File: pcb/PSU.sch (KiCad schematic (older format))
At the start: 18 parts, among them Q3 DMG2305UX, Q4 BCM857BS, U18 XCL206B123, U9 AP7361C-33-FGE

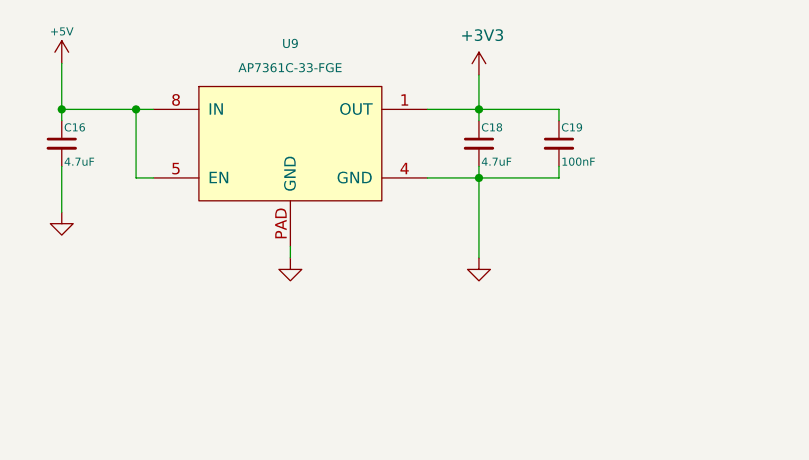
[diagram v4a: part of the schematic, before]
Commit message: 3v3 torex reg
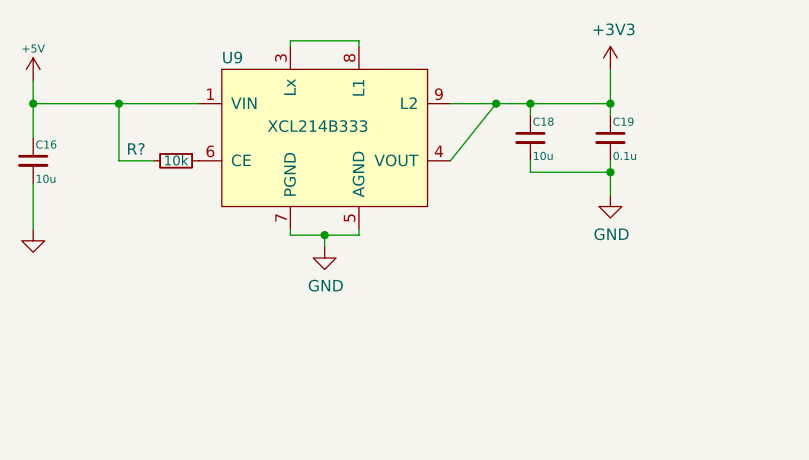
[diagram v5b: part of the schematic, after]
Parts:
- removed U9: AP7361C-33-FGE, SMD:8DFN, symbol ap7361c:AP7361C-33-ap7361c-33
- added R?: 10k, Resistor_SMD:R_0402_1005Metric, symbol Device:R_Small
- added U9: XCL214B333, symbol torex:XCL214
- C16, C18: value 4.7uF -> 10u
- C19: value 100nF -> 0.1u
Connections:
- net +3V3: now also U9.4 (VOUT), U9.9 (L2)
- net +5V: now also R?.2, U9.1 (VIN)
- net GND: now also U9.5 (AGND), U9.7 (PGND)
- new net: U9.3 (Lx), U9.8 (L1)
- new net: R?.1, U9.6 (CE)
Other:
- moved on the sheet: C16, C18, C19
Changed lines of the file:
@@
 L power:+5V #PWR0111
 U 1 1 590BB025
-P 1750 1800
-F 0 "#PWR0111" H 1750 1650 35  0001 C CNN
-F 1 "+5V" H 1750 1940 35  0000 C CNN
-F 2 "" H 1750 1800 60  0000 C CNN
-F 3 "" H 1750 1800 60  0000 C CNN
-	1    1750 1800
-	1    0    0    -1
-$EndComp
-$Comp
-L Device:C_Small C18
-U 1 1 590BB02B
-P 3575 2150
-F 0 "C18" H 3585 2220 35  0000 L CNN
-F 1 "4.7uF" H 3585 2070 35  0000 L CNN
-F 2 "Capacitors_SMD:C_0603" H 3575 2150 60  0001 C CNN
-F 3 "" H 3575 2150 60  0000 C CNN
-	1    3575 2150
-	1    0    0    -1
-$EndComp
-$Comp
-L power:GND #PWR0112
-U 1 1 590BB032
-P 3575 2650
-F 0 "#PWR0112" H 3575 2650 30  0001 C CNN
-F 1 "GND" H 3575 2580 30  0001 C CNN
-F 2 "" H 3575 2650 60  0000 C CNN
-F 3 "" H 3575 2650 60  0000 C CNN
-	1    3575 2650
+P 1625 1875
+F 0 "#PWR0111" H 1625 1725 35  0001 C CNN
+F 1 "+5V" H 1625 2015 35  0000 C CNN
+F 2 "" H 1625 1875 60  0000 C CNN
+F 3 "" H 1625 1875 60  0000 C CNN
+	1    1625 1875
 	1    0    0    -1
 $EndComp
@@
 L power:GND #PWR0116
 U 1 1 590BB038
-P 1750 2450
-F 0 "#PWR0116" H 1750 2450 30  0001 C CNN
-F 1 "GND" H 1750 2380 30  0001 C CNN
-F 2 "" H 1750 2450 60  0000 C CNN
-F 3 "" H 1750 2450 60  0000 C CNN
-	1    1750 2450
+P 1625 2525
+F 0 "#PWR0116" H 1625 2525 30  0001 C CNN
+F 1 "GND" H 1625 2455 30  0001 C CNN
+F 2 "" H 1625 2525 60  0000 C CNN
+F 3 "" H 1625 2525 60  0000 C CNN
+	1    1625 2525
 	1    0    0    -1
 $EndComp
@@
 L Device:C_Small C16
 U 1 1 590BB03E
-P 1750 2150
-F 0 "C16" H 1760 2220 35  0000 L CNN
-F 1 "4.7uF" H 1760 2070 35  0000 L CNN
-F 2 "Capacitors_SMD:C_0603" H 1750 2150 60  0001 C CNN
-F 3 "" H 1750 2150 60  0000 C CNN
-	1    1750 2150
-	1    0    0    -1
-$EndComp
-$Comp
-L power:GND #PWR0117
-U 1 1 590BB04C
-P 2750 2650
-F 0 "#PWR0117" H 2750 2650 30  0001 C CNN
-F 1 "GND" H 2750 2580 30  0001 C CNN
-F 2 "" H 2750 2650 60  0000 C CNN
-F 3 "" H 2750 2650 60  0000 C CNN
-	1    2750 2650
-	1    0    0    -1
-$EndComp
-$Comp
-L Device:C_Small C19
-U 1 1 590BB065
-P 3925 2150
-F 0 "C19" H 3935 2220 35  0000 L CNN
-F 1 "100nF" H 3935 2070 35  0000 L CNN
-F 2 "Capacitors_SMD:C_0402" H 3925 2150 60  0001 C CNN
-F 3 "" H 3925 2150 60  0000 C CNN
-	1    3925 2150
-	1    0    0    -1
-$EndComp
-$Comp
-L ap7361c:AP7361C-33-ap7361c-33 U9
-U 1 1 590BB045
-P 2750 2200
-F 0 "U9" H 2750 2687 39  0000 C CNN
-F 1 "AP7361C-33-FGE" H 2750 2581 39  0000 C CNN
-F 2 "SMD:8DFN" H 2700 2200 60  0001 C CNN
-F 3 "" H 2700 2200 60  0001 C CNN
-	1    2750 2200
+P 1625 2225
+F 0 "C16" H 1635 2295 35  0000 L CNN
+F 1 "10u" H 1635 2145 35  0000 L CNN
+F 2 "Capacitors_SMD:C_0603" H 1625 2225 60  0001 C CNN
+F 3 "" H 1625 2225 60  0000 C CNN
+	1    1625 2225
 	1    0    0    -1
 $EndComp
@@
 	1    0    0    -1
 $EndComp
-Connection ~ 1750 2000
-Wire Wire Line
-	1750 2000 2075 2000
-Wire Wire Line
-	1750 1800 1750 2000
-Connection ~ 3575 2000
-Wire Wire Line
-	3575 1850 3575 2000
-Connection ~ 3575 2300
-Wire Wire Line
-	3350 2300 3575 2300
-Wire Wire Line
-	3575 2250 3575 2300
-Wire Wire Line
-	2750 2600 2750 2650
-Wire Wire Line
-	1750 2250 1750 2450
-Wire Wire Line
-	2150 2300 2075 2300
-Wire Wire Line
-	2075 2300 2075 2000
-Connection ~ 2075 2000
-Wire Wire Line
-	3350 2000 3575 2000
-Wire Wire Line
-	3925 2300 3925 2250
-Wire Wire Line
-	3925 2050 3925 2000
+Wire Wire Line
+	1625 2325 1625 2525
 Wire Wire Line
 	1900 4875 2050 4875
@@
 	5050 4950 5050 4900
 Wire Wire Line
-	1750 2000 1750 2050
-Wire Wire Line
-	3575 2000 3575 2050
-Wire Wire Line
-	3575 2000 3925 2000
-Wire Wire Line
-	3575 2300 3925 2300
-Wire Wire Line
-	3575 2300 3575 2650
-Wire Wire Line
-	2075 2000 2150 2000
-Wire Wire Line
 	2675 4875 2750 4875
 Wire Wire Line
@@
 L power:+3V3 #PWR0224
 U 1 1 5EA96191
-P 3575 1850
-F 0 "#PWR0224" H 3575 1700 50  0001 C CNN
-F 1 "+3V3" H 3590 2023 50  0000 C CNN
-F 2 "" H 3575 1850 50  0001 C CNN
-F 3 "" H 3575 1850 50  0001 C CNN
-	1    3575 1850
+P 4150 1825
+F 0 "#PWR0224" H 4150 1675 50  0001 C CNN
+F 1 "+3V3" H 4165 1998 50  0000 C CNN
+F 2 "" H 4150 1825 50  0001 C CNN
+F 3 "" H 4150 1825 50  0001 C CNN
+	1    4150 1825
 	1    0    0    -1
 $EndComp
@@
 Wire Wire Line
 	6550 1900 6550 1925
+$Comp
+L torex:XCL214 U9
+U 1 1 5EE15428
+P 2900 2125
+F 0 "U9" H 2450 2475 50  0000 L CNN
+F 1 "XCL214B333" H 2650 2175 50  0000 L CNN
+F 2 "" H 2900 2125 50  0001 C CNN
+F 3 "" H 2900 2125 50  0001 C CNN
+F 4 " 893-1218-6-ND " H 2900 2125 50  0001 C CNN "DigiKey"
+	1    2900 2125
+	1    0    0    -1
+$EndComp
+Wire Wire Line
+	3450 1975 3650 1975
+Wire Wire Line
+	3450 2225 3650 1975
+Wire Wire Line
+	2750 1725 2750 1700
+Wire Wire Line
+	2750 1700 3050 1700
+Wire Wire Line
+	3050 1700 3050 1725
+Wire Wire Line
+	2750 2525 2750 2550
+Wire Wire Line
+	2750 2550 2900 2550
+Wire Wire Line
+	3050 2550 3050 2525
+Wire Wire Line
+	2900 2550 2900 2600
+Connection ~ 2900 2550
+Wire Wire Line
+	2900 2550 3050 2550
+$Comp
+L power:GND #PWR?
+U 1 1 5EE35BB4
+P 2900 2600
+F 0 "#PWR?" H 2900 2350 50  0001 C CNN
+F 1 "GND" H 2905 2427 50  0000 C CNN
+F 2 "" H 2900 2600 50  0001 C CNN
+F 3 "" H 2900 2600 50  0001 C CNN
+	1    2900 2600
+	1    0    0    -1
+$EndComp
+$Comp
+L Device:C_Small C18
+U 1 1 590BB02B
+P 3800 2125
+F 0 "C18" H 3810 2195 35  0000 L CNN
+F 1 "10u" H 3810 2045 35  0000 L CNN
+F 2 "Capacitors_SMD:C_0603" H 3800 2125 60  0001 C CNN
+F 3 "" H 3800 2125 60  0000 C CNN
+	1    3800 2125
+	1    0    0    -1
+$EndComp
+Wire Wire Line
+	3800 1975 3800 2025
+Wire Wire Line
+	3800 2275 4150 2275
+Wire Wire Line
+	3800 1975 4150 1975
+Wire Wire Line
+	4150 2025 4150 1975
+Wire Wire Line
+	4150 2275 4150 2225
+Wire Wire Line
+	3800 2225 3800 2275
+Connection ~ 4150 1975
+Wire Wire Line
+	4150 1825 4150 1975
+$Comp
+L Device:C_Small C19
+U 1 1 590BB065
+P 4150 2125
+F 0 "C19" H 4160 2195 35  0000 L CNN
+F 1 "0.1u" H 4160 2045 35  0000 L CNN
+F 2 "Capacitors_SMD:C_0402" H 4150 2125 60  0001 C CNN
+F 3 "" H 4150 2125 60  0000 C CNN
+	1    4150 2125
+	1    0    0    -1
+$EndComp
+Wire Wire Line
+	3650 1975 3800 1975
+Connection ~ 3650 1975
+Connection ~ 3800 1975
+Wire Wire Line
+	4150 2275 4150 2375
+Connection ~ 4150 2275
+$Comp
+L power:GND #PWR?
+U 1 1 5EE597F6
+P 4150 2375
+F 0 "#PWR?" H 4150 2125 50  0001 C CNN
+F 1 "GND" H 4155 2202 50  0000 C CNN
+F 2 "" H 4150 2375 50  0001 C CNN
+F 3 "" H 4150 2375 50  0001 C CNN
+	1    4150 2375
+	1    0    0    -1
+$EndComp
+$Comp
+L Device:R_Small R?
+U 1 1 5EE5CC96
+P 2250 2225
+F 0 "R?" V 2200 2050 50  0000 C CNN
+F 1 "10k" V 2250 2225 43  0000 C CNN
+F 2 "Resistor_SMD:R_0402_1005Metric" H 2250 2225 50  0001 C CNN
+F 3 "~" H 2250 2225 50  0001 C CNN
+	1    2250 2225
+	0    1    1    0
+$EndComp
+Wire Wire Line
+	2000 2225 2150 2225
+Wire Wire Line
+	2350 1975 2000 1975
+Wire Wire Line
+	2000 1975 2000 2225
+Wire Wire Line
+	1625 1875 1625 1975
+Wire Wire Line
+	2000 1975 1625 1975
+Connection ~ 2000 1975
+Connection ~ 1625 1975
+Wire Wire Line
+	1625 1975 1625 2125
 $EndSCHEMATC

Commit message: torex dc-dc module
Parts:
- U9: footprint (none) -> SMD:TOREX_XCL214B123DR
- gave numbers to parts that had none: 1
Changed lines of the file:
@@
 EESchema Schematic File Version 4
+LIBS:keep_breathing_ctrl-cache
 EELAYER 30 0
 EELAYER END
@@
 F 0 "U9" H 2450 2475 50  0000 L CNN
 F 1 "XCL214B333" H 2650 2175 50  0000 L CNN
-F 2 "" H 2900 2125 50  0001 C CNN
+F 2 "SMD:TOREX_XCL214B123DR" H 2900 2125 50  0001 C CNN
 F 3 "" H 2900 2125 50  0001 C CNN
 F 4 " 893-1218-6-ND " H 2900 2125 50  0001 C CNN "DigiKey"
@@
 	2900 2550 3050 2550
 $Comp
-L power:GND #PWR?
+L power:GND #PWR0112
 U 1 1 5EE35BB4
 P 2900 2600
-F 0 "#PWR?" H 2900 2350 50  0001 C CNN
+F 0 "#PWR0112" H 2900 2350 50  0001 C CNN
 F 1 "GND" H 2905 2427 50  0000 C CNN
 F 2 "" H 2900 2600 50  0001 C CNN
@@
 Connection ~ 4150 2275
 $Comp
-L power:GND #PWR?
+L power:GND #PWR0117
 U 1 1 5EE597F6
 P 4150 2375
-F 0 "#PWR?" H 4150 2125 50  0001 C CNN
+F 0 "#PWR0117" H 4150 2125 50  0001 C CNN
 F 1 "GND" H 4155 2202 50  0000 C CNN
 F 2 "" H 4150 2375 50  0001 C CNN
@@
 $EndComp
 $Comp
-L Device:R_Small R?
+L Device:R_Small R43
 U 1 1 5EE5CC96
 P 2250 2225
-F 0 "R?" V 2200 2050 50  0000 C CNN
+F 0 "R43" V 2200 2050 50  0000 C CNN
 F 1 "10k" V 2250 2225 43  0000 C CNN
 F 2 "Resistor_SMD:R_0402_1005Metric" H 2250 2225 50  0001 C CNN

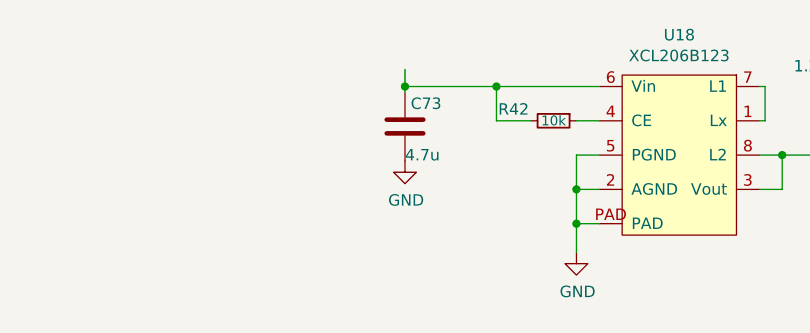
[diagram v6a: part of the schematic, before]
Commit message: ferrite bead added
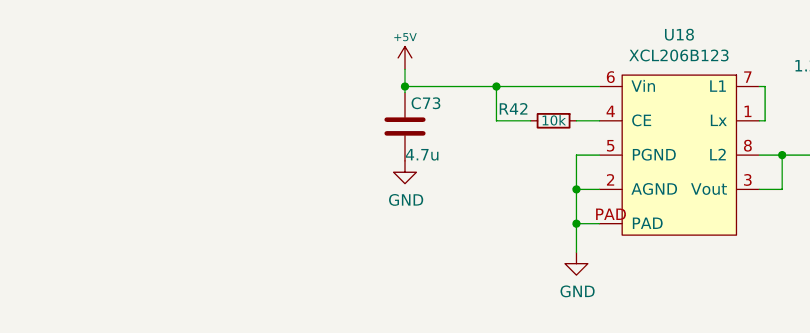
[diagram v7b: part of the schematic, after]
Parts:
- C16, C18: footprint Capacitors_SMD:C_0603 -> Capacitor_SMD:C_0603_1608Metric
- C19: footprint Capacitors_SMD:C_0402 -> Capacitor_SMD:C_0402_1005Metric
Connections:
- net +5V: now also C73.1, R42.2, U18.6 (Vin)
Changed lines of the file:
@@
 EESchema Schematic File Version 4
-LIBS:keep_breathing_ctrl-cache
 EELAYER 30 0
 EELAYER END
@@
 F 0 "C16" H 1635 2295 35  0000 L CNN
 F 1 "10u" H 1635 2145 35  0000 L CNN
-F 2 "Capacitors_SMD:C_0603" H 1625 2225 60  0001 C CNN
+F 2 "Capacitor_SMD:C_0603_1608Metric" H 1625 2225 60  0001 C CNN
 F 3 "" H 1625 2225 60  0000 C CNN
 	1    1625 2225
@@
 F 0 "C18" H 3810 2195 35  0000 L CNN
 F 1 "10u" H 3810 2045 35  0000 L CNN
-F 2 "Capacitors_SMD:C_0603" H 3800 2125 60  0001 C CNN
+F 2 "Capacitor_SMD:C_0603_1608Metric" H 3800 2125 60  0001 C CNN
 F 3 "" H 3800 2125 60  0000 C CNN
 	1    3800 2125
@@
 F 0 "C19" H 4160 2195 35  0000 L CNN
 F 1 "0.1u" H 4160 2045 35  0000 L CNN
-F 2 "Capacitors_SMD:C_0402" H 4150 2125 60  0001 C CNN
+F 2 "Capacitor_SMD:C_0402_1005Metric" H 4150 2125 60  0001 C CNN
 F 3 "" H 4150 2125 60  0000 C CNN
 	1    4150 2125
@@
 Wire Wire Line
 	1625 1975 1625 2125
+$Comp
+L power:+5V #PWR?
+U 1 1 5EAF9782
+P 6550 1825
+F 0 "#PWR?" H 6550 1675 35  0001 C CNN
+F 1 "+5V" H 6550 1965 35  0000 C CNN
+F 2 "" H 6550 1825 60  0000 C CNN
+F 3 "" H 6550 1825 60  0000 C CNN
+	1    6550 1825
+	1    0    0    -1
+$EndComp
 $EndSCHEMATC

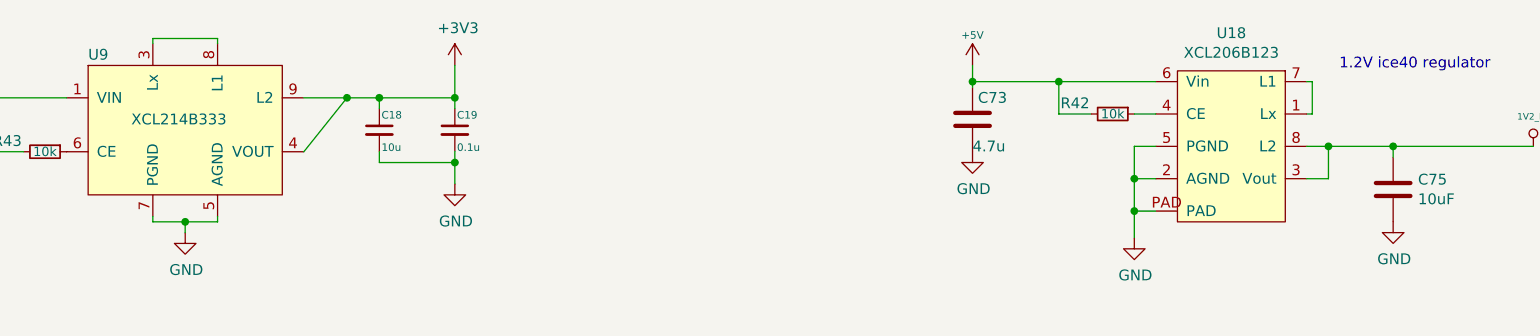
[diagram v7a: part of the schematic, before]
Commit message: XCL214 placement
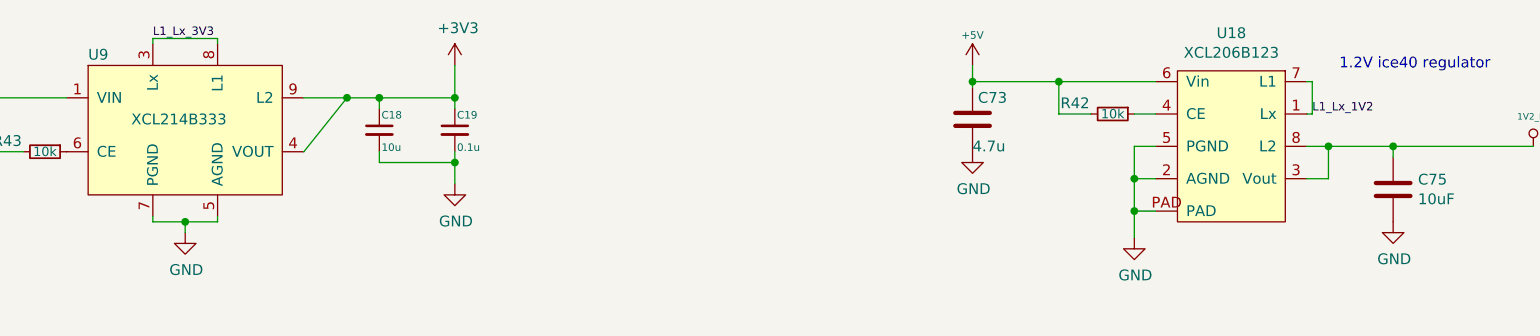
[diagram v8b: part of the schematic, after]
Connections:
- net L1_Lx_1V2: now reaches U18.1 (Lx), U18.7 (L1)
- net L1_Lx_3V3: now reaches U9.3 (Lx), U9.8 (L1)
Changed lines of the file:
@@
 	1625 1975 1625 2125
 $Comp
-L power:+5V #PWR?
+L power:+5V #PWR0225
 U 1 1 5EAF9782
 P 6550 1825
-F 0 "#PWR?" H 6550 1675 35  0001 C CNN
+F 0 "#PWR0225" H 6550 1675 35  0001 C CNN
 F 1 "+5V" H 6550 1965 35  0000 C CNN
 F 2 "" H 6550 1825 60  0000 C CNN
@@
 	1    0    0    -1
 $EndComp
+Text Label 8125 2050 0    39   ~ 0
+L1_Lx_1V2
+Text Label 2750 1700 0    39   ~ 0
+L1_Lx_3V3
 $EndSCHEMATC
